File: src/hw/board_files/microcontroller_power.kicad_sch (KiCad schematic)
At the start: 32 parts, among them J3 Conn_ARM_SWD_TagConnect_TC203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, J7 JST??, SW1 RESET, U2 W25Q32JVSS, U4 MDBT50Q-1MV2, U5 BQ24074RGT, U9 XC6220B331MR, Y3 32.768kHz

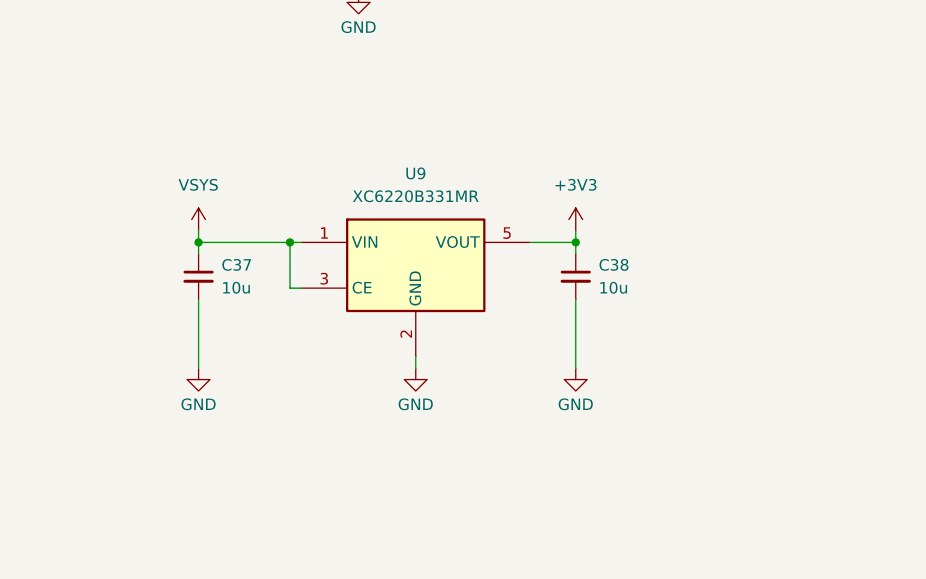
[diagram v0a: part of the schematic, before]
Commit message: Added power switch
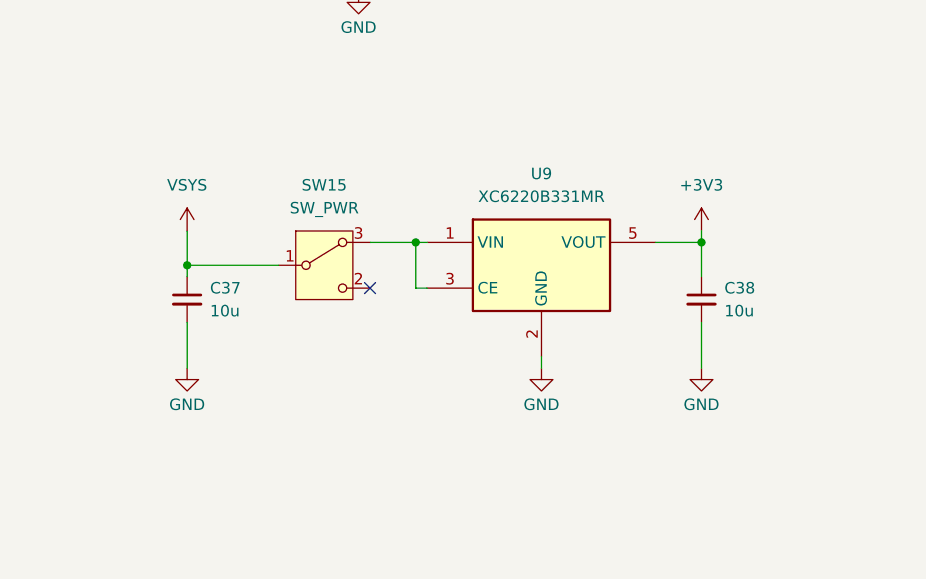
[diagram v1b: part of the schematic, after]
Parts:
- added SW15: SW_PWR, Button_Switch_THT:SW_Slide-03_Wuerth-WS-SLTV_10x2.5x6.4_P2.54mm, symbol Switch:SW_Wuerth_450301014042
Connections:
- net VSYS: now also SW15.1 (B); no longer U9.1 (VIN), U9.3 (CE)
- new net: SW15.3 (A), U9.1 (VIN), U9.3 (CE)
- no-connect marks 10 -> 11
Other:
- moved on the sheet: C37, C38, U9

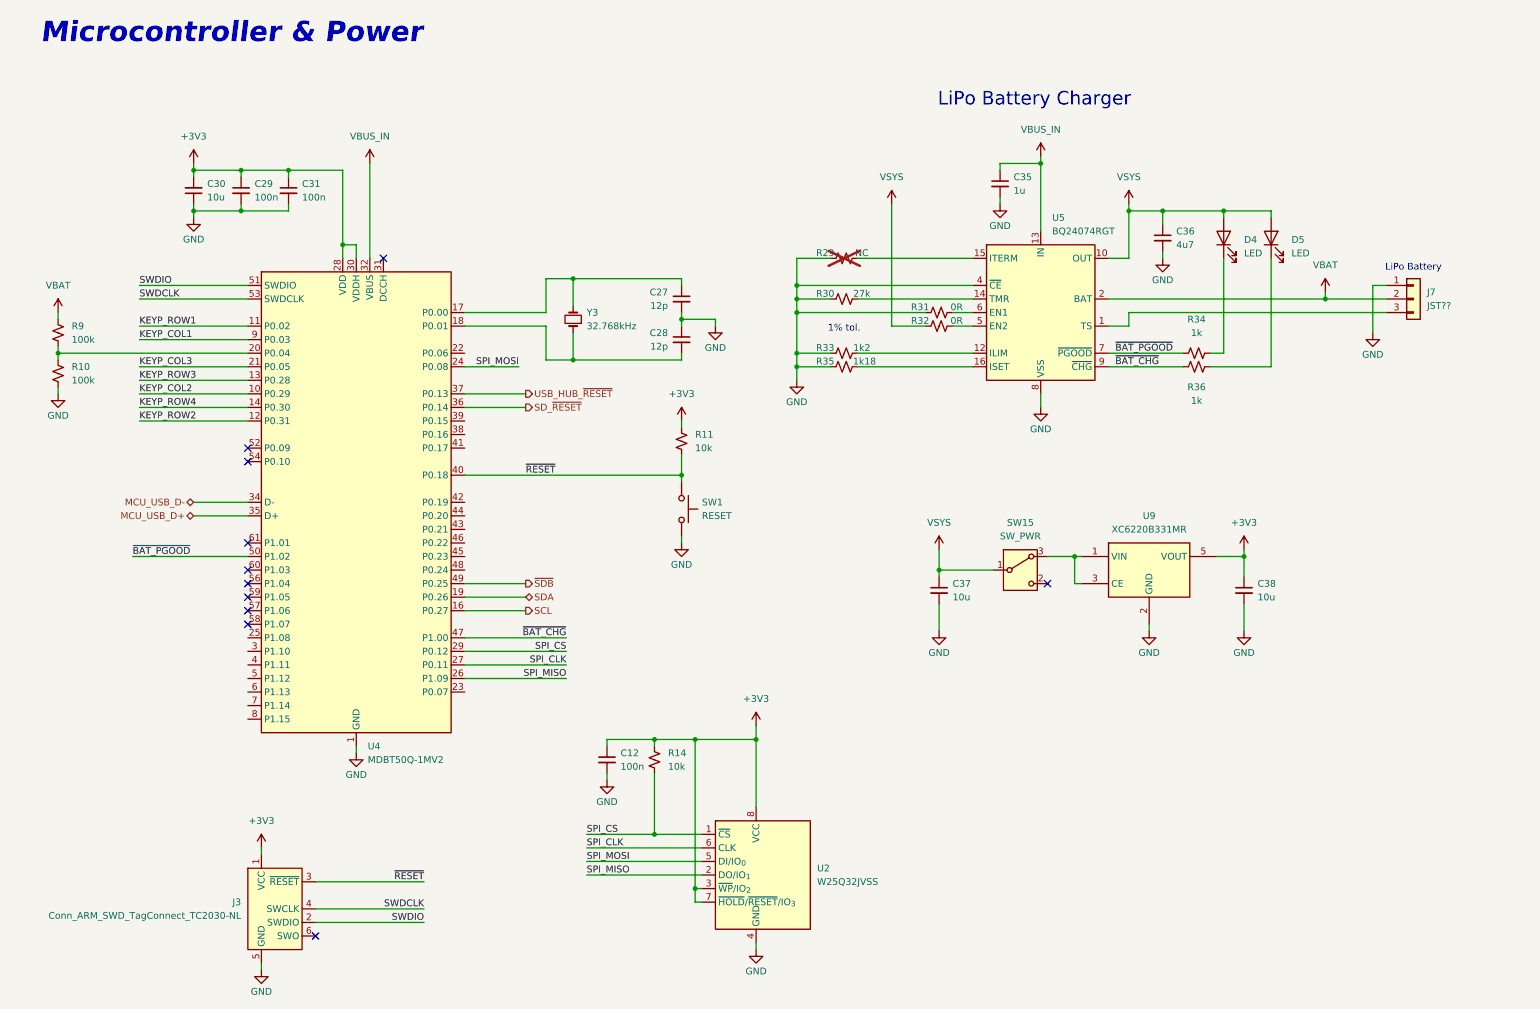
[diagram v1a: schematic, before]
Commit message: Added all footprints, need to connect switches to MCU
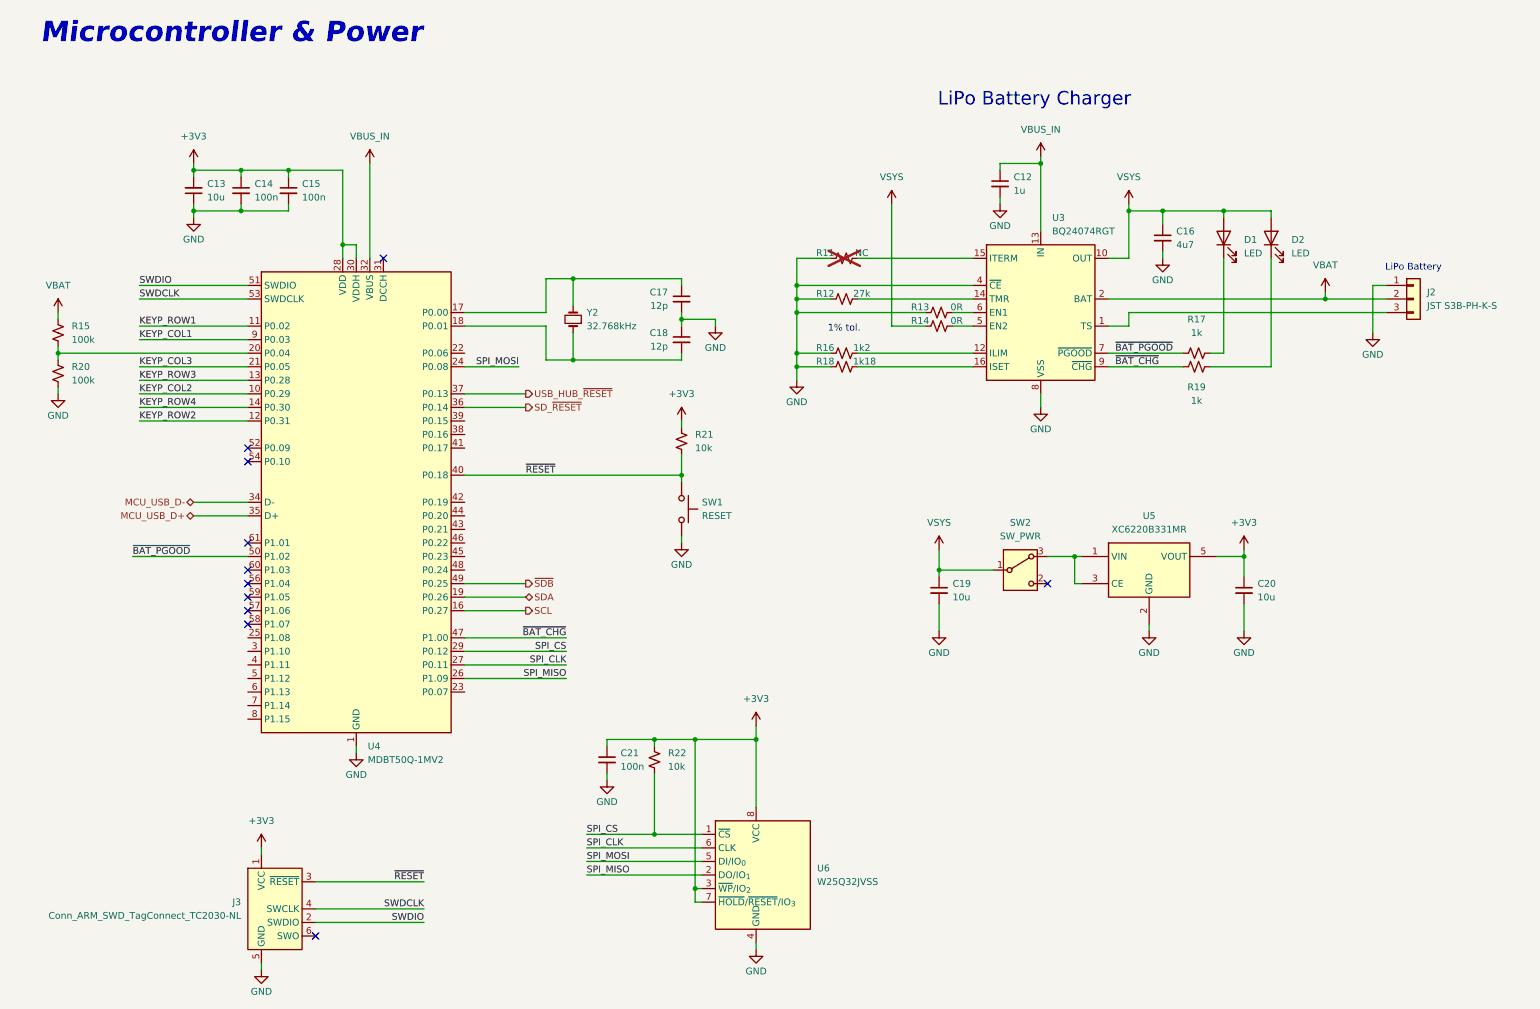
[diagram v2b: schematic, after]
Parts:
- C12: renamed from C35; footprint (none) -> Capacitor_SMD:C_0603_1608Metric_Pad1.08x0.95mm_HandSolder
- C13: renamed from C30; footprint (none) -> Capacitor_SMD:C_0805_2012Metric_Pad1.18x1.45mm_HandSolder
- C14: renamed from C29; footprint (none) -> Capacitor_SMD:C_0603_1608Metric_Pad1.08x0.95mm_HandSolder
- C15: renamed from C31; footprint (none) -> Capacitor_SMD:C_0603_1608Metric_Pad1.08x0.95mm_HandSolder
- C16: renamed from C36; footprint (none) -> Capacitor_SMD:C_0805_2012Metric_Pad1.18x1.45mm_HandSolder
- C17: renamed from C27; footprint (none) -> Capacitor_SMD:C_0603_1608Metric_Pad1.08x0.95mm_HandSolder
- C18: renamed from C28; footprint (none) -> Capacitor_SMD:C_0603_1608Metric_Pad1.08x0.95mm_HandSolder
- C19: renamed from C37; footprint (none) -> Capacitor_SMD:C_0805_2012Metric_Pad1.18x1.45mm_HandSolder
- C20: renamed from C38; footprint (none) -> Capacitor_SMD:C_0805_2012Metric_Pad1.18x1.45mm_HandSolder
- C21: renamed from C12; footprint (none) -> Capacitor_SMD:C_0603_1608Metric_Pad1.08x0.95mm_HandSolder
- D1: renamed from D4; footprint (none) -> LED_SMD:LED_0603_1608Metric_Pad1.05x0.95mm_HandSolder
- D2: renamed from D5; footprint (none) -> LED_SMD:LED_0603_1608Metric_Pad1.05x0.95mm_HandSolder
- J2: renamed from J7; value JST?? -> JST S3B-PH-K-S; footprint (none) -> Connector_JST:JST_PH_S3B-PH-K_1x03_P2.00mm_Horizontal
- R11: renamed from R29; footprint (none) -> Resistor_SMD:R_0805_2012Metric_Pad1.20x1.40mm_HandSolder
- R12: renamed from R30; footprint (none) -> Resistor_SMD:R_0805_2012Metric_Pad1.20x1.40mm_HandSolder
- R13: renamed from R31; footprint (none) -> Resistor_SMD:R_0805_2012Metric_Pad1.20x1.40mm_HandSolder
- R14: renamed from R32; footprint (none) -> Resistor_SMD:R_0805_2012Metric_Pad1.20x1.40mm_HandSolder
- R15: renamed from R9; footprint (none) -> Resistor_SMD:R_0603_1608Metric_Pad0.98x0.95mm_HandSolder
- R16: renamed from R33; footprint (none) -> Resistor_SMD:R_0805_2012Metric_Pad1.20x1.40mm_HandSolder
- R17: renamed from R34; footprint (none) -> Resistor_SMD:R_0805_2012Metric_Pad1.20x1.40mm_HandSolder
- R18: renamed from R35; footprint (none) -> Resistor_SMD:R_0805_2012Metric_Pad1.20x1.40mm_HandSolder
- R19: renamed from R36; footprint (none) -> Resistor_SMD:R_0805_2012Metric_Pad1.20x1.40mm_HandSolder
- R20: renamed from R10; footprint (none) -> Resistor_SMD:R_0603_1608Metric_Pad0.98x0.95mm_HandSolder
- R21: renamed from R11; footprint (none) -> Resistor_SMD:R_0805_2012Metric_Pad1.20x1.40mm_HandSolder
- R22: renamed from R14; footprint (none) -> Resistor_SMD:R_0805_2012Metric_Pad1.20x1.40mm_HandSolder
- Y2: renamed from Y3; footprint (none) -> Crystal:Crystal_SMD_3215-2Pin_3.2x1.5mm
- renumbered SW15 to SW2, U5 to U3, U9 to U5, U2 to U6
